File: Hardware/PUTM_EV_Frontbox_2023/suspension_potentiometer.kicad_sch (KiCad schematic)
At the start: 19 parts, among them U13 MCP6001, U9 MCP6N11-005

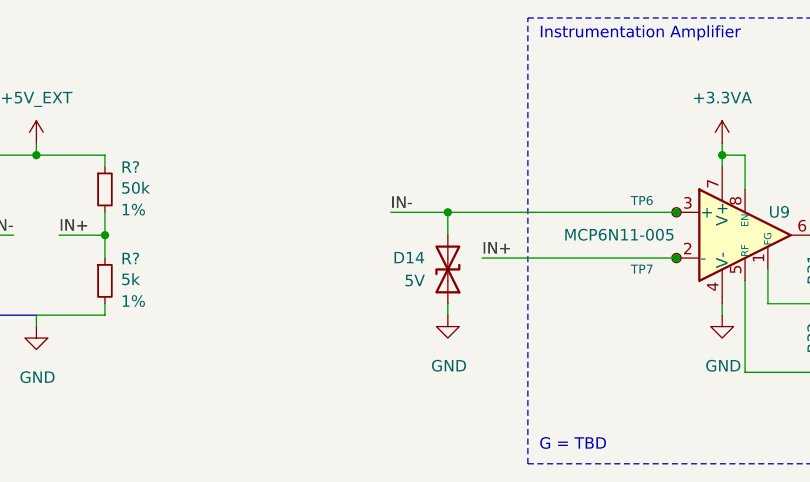
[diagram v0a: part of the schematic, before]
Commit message: Schematic updates
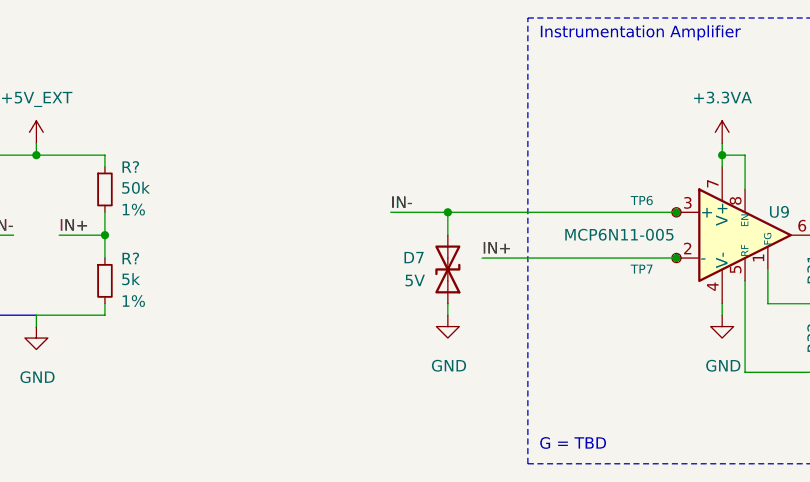
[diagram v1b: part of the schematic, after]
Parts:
- renumbered D14 to D7, NT4 to NT1
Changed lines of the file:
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@@
   (symbol (lib_id "Device:R_Small") (at 146.05 93.345 180) (unit 1)
     (in_bom yes) (on_board yes) (dnp no)
-    (property "Reference" "R?" (at 143.51 93.345 90)
+    (property "Reference" "R31" (at 143.51 93.345 90)
       (effects (font (size 1.27 1.27)))
     )
@@
   (symbol (lib_id "Connector:TestPoint_Small") (at 128.27 86.995 0) (unit 1)
     (in_bom yes) (on_board yes) (dnp no)
-    (property "Reference" "TP?" (at 123.19 85.725 0)
+    (property "Reference" "TP6" (at 123.19 85.725 0)
       (effects (font (size 1 1)) (justify left))
     )
@@
   (symbol (lib_id "power:GND") (at 182.88 100.965 0) (unit 1)
     (in_bom yes) (on_board yes) (dnp no)
-    (property "Reference" "#PWR?" (at 182.88 107.315 0)
+    (property "Reference" "#PWR033" (at 182.88 107.315 0)
       (effects (font (size 1.27 1.27)) hide)
     )
@@
   (symbol (lib_id "power:GND") (at 196.85 100.965 0) (unit 1)
     (in_bom yes) (on_board yes) (dnp no)
-    (property "Reference" "#PWR?" (at 196.85 107.315 0)
+    (property "Reference" "#PWR063" (at 196.85 107.315 0)
       (effects (font (size 1.27 1.27)) hide)
     )
@@
   (symbol (lib_id "power:GND") (at 102.87 98.425 0) (unit 1)
     (in_bom yes) (on_board yes) (dnp no)
-    (property "Reference" "#PWR?" (at 102.87 104.775 0)
+    (property "Reference" "#PWR024" (at 102.87 104.775 0)
       (effects (font (size 1.27 1.27)) hide)
     )
@@
   (symbol (lib_id "Device:R_Small") (at 163.83 89.535 90) (unit 1)
     (in_bom yes) (on_board yes) (dnp no)
-    (property "Reference" "R?" (at 163.83 86.995 90)
+    (property "Reference" "R33" (at 163.83 86.995 90)
       (effects (font (size 1.27 1.27)))
     )
@@
   (symbol (lib_id "power:GND") (at 133.35 98.425 0) (unit 1)
     (in_bom yes) (on_board yes) (dnp no)
-    (property "Reference" "#PWR?" (at 133.35 104.775 0)
+    (property "Reference" "#PWR030" (at 133.35 104.775 0)
       (effects (font (size 1.27 1.27)) hide)
     )
@@
   (symbol (lib_id "Device:NetTie_2") (at 46.99 89.535 0) (unit 1)
     (in_bom no) (on_board yes) (dnp no) (fields_autoplaced)
-    (property "Reference" "NT4" (at 46.99 84.455 0)
+    (property "Reference" "NT1" (at 46.99 84.455 0)
       (effects (font (size 1.27 1.27)) hide)
     )
@@
   (symbol (lib_id "MCP6N11:MCP6N11") (at 135.89 89.535 0) (unit 1)
     (in_bom yes) (on_board yes) (dnp no)
-    (property "Reference" "U?" (at 139.7 86.995 0)
+    (property "Reference" "U9" (at 139.7 86.995 0)
       (effects (font (size 1.27 1.27)))
     )
@@
   (symbol (lib_id "Amplifier_Operational:MCP6001-OT") (at 199.39 92.075 0) (unit 1)
     (in_bom yes) (on_board yes) (dnp no)
-    (property "Reference" "U?" (at 201.93 88.6461 0)
+    (property "Reference" "U13" (at 201.93 88.6461 0)
       (effects (font (size 1.27 1.27)))
     )
@@
   (symbol (lib_id "Connector:TestPoint_Small") (at 128.27 92.075 0) (mirror x) (unit 1)
     (in_bom yes) (on_board yes) (dnp no)
-    (property "Reference" "TP?" (at 123.19 93.345 0)
+    (property "Reference" "TP7" (at 123.19 93.345 0)
       (effects (font (size 1 1)) (justify left))
     )
@@
   (symbol (lib_id "Connector:TestPoint_Small") (at 208.28 92.075 0) (unit 1)
     (in_bom yes) (on_board yes) (dnp no)
-    (property "Reference" "TP?" (at 209.55 90.805 0)
+    (property "Reference" "TP9" (at 209.55 90.805 0)
       (effects (font (size 1 1)) (justify left))
     )
@@
   (symbol (lib_id "Device:R_Small") (at 146.05 100.965 180) (unit 1)
     (in_bom yes) (on_board yes) (dnp no)
-    (property "Reference" "R?" (at 143.51 100.965 90)
+    (property "Reference" "R32" (at 143.51 100.965 90)
       (effects (font (size 1.27 1.27)))
     )
@@
   (symbol (lib_id "power:GND") (at 241.3 97.155 0) (unit 1)
     (in_bom yes) (on_board yes) (dnp no)
-    (property "Reference" "#PWR?" (at 241.3 103.505 0)
+    (property "Reference" "#PWR092" (at 241.3 103.505 0)
       (effects (font (size 1.27 1.27)) hide)
     )
@@
   (symbol (lib_id "Device:R_Small") (at 173.99 89.535 90) (unit 1)
     (in_bom yes) (on_board yes) (dnp no)
-    (property "Reference" "R?" (at 173.99 86.995 90)
+    (property "Reference" "R34" (at 173.99 86.995 90)
       (effects (font (size 1.27 1.27)))
     )
@@
   (symbol (lib_id "Device:C_Small") (at 189.23 75.565 90) (unit 1)
     (in_bom yes) (on_board yes) (dnp no)
-    (property "Reference" "C?" (at 191.1413 71.755 90)
+    (property "Reference" "C21" (at 191.1413 71.755 90)
       (effects (font (size 1.27 1.27)) (justify left))
     )
@@
   (symbol (lib_id "Power_Ports:+5V_EXT") (at 57.15 79.375 0) (unit 1)
     (in_bom yes) (on_board yes) (dnp no)
-    (property "Reference" "#PWR051" (at 57.15 83.185 0)
+    (property "Reference" "#PWR019" (at 57.15 83.185 0)
       (effects (font (size 1.27 1.27)) hide)
     )
@@
   (symbol (lib_id "Device:C_Small") (at 182.88 95.885 0) (mirror y) (unit 1)
     (in_bom yes) (on_board yes) (dnp no)
-    (property "Reference" "C?" (at 180.34 95.2563 0)
+    (property "Reference" "C2" (at 180.34 95.2563 0)
       (effects (font (size 1.27 1.27)) (justify left))
     )
@@
   (symbol (lib_id "Device:D_TVS") (at 102.87 93.345 270) (mirror x) (unit 1)
     (in_bom yes) (on_board yes) (dnp no)
-    (property "Reference" "D14" (at 100.33 92.075 90)
+    (property "Reference" "D7" (at 100.33 92.075 90)
       (effects (font (size 1.27 1.27)) (justify right))
     )
@@
   (symbol (lib_id "Connector:TestPoint_Small") (at 146.05 89.535 0) (unit 1)
     (in_bom yes) (on_board yes) (dnp no)
-    (property "Reference" "TP?" (at 144.78 88.265 0)
+    (property "Reference" "TP8" (at 144.78 88.265 0)
       (effects (font (size 1 1)) (justify left))
     )
@@
   (symbol (lib_id "Device:C_Small") (at 246.38 92.075 0) (unit 1)
     (in_bom yes) (on_board yes) (dnp no)
-    (property "Reference" "C?" (at 248.92 91.4463 0)
+    (property "Reference" "C26" (at 248.92 91.4463 0)
       (effects (font (size 1.27 1.27)) (justify left))
     )
@@
   (symbol (lib_id "power:GND") (at 146.05 106.045 0) (unit 1)
     (in_bom yes) (on_board yes) (dnp no)
-    (property "Reference" "#PWR?" (at 146.05 112.395 0)
+    (property "Reference" "#PWR031" (at 146.05 112.395 0)
       (effects (font (size 1.27 1.27)) hide)
     )
@@
   (symbol (lib_id "Device:C_Small") (at 236.22 92.075 0) (unit 1)
     (in_bom yes) (on_board yes) (dnp no)
-    (property "Reference" "C?" (at 238.76 91.4463 0)
-      (effects (font (size 1.27 1.27)) (justify left))
-    )
+    (property "Reference" "C22" (at 238.76 91.4463 0)
+      (effects (font (size 1.27 1.27)) (justify left))
+    )

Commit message: Started PCB layout
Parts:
- removed NT1: NetTie_2, NetTie:NetTie-2_SMD_Pad0.5mm, symbol Device:NetTie_2
- C31: renamed from C26; footprint Capacitor_SMD:C_0603_1608Metric -> Capacitor_SMD:C_0402_1005Metric_Pad0.74x0.62mm_HandSolder
- renumbered C2 to C27, C21 to C28, C22 to C30, D7 to D8, R31 to R44, R32 to R45, R33 to R46, R34 to R47, TP6 to TP10, TP7 to TP11, TP8 to TP12, TP9 to TP13, U9 to U14, U13 to U15
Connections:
- net IN- is gone; now on net IN: D8.2 (A2), R?.2, TP10.1, U14.3 (+)

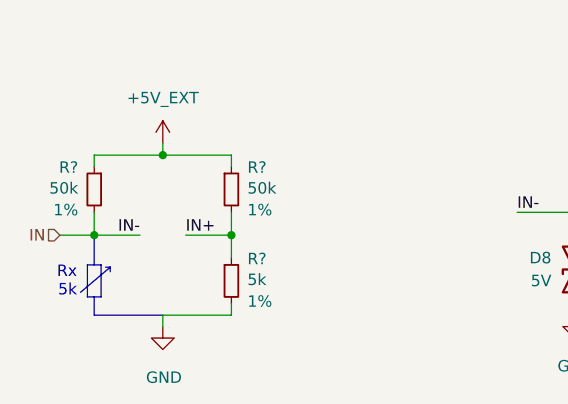
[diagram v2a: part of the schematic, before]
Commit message: Changed board outline and layout to match ASB
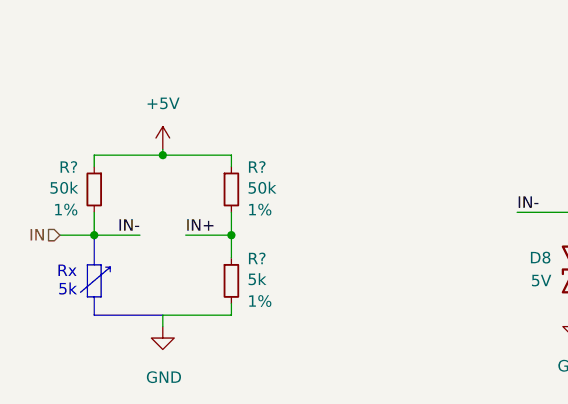
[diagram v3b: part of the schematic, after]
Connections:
- net +5V_EXT renamed +5V
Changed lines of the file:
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@@
     (stroke (width 0) (type default))
   )
-  (wire (pts (xy 57.15 79.375) (xy 57.15 80.645))
+  (wire (pts (xy 57.15 80.01) (xy 57.15 80.645))
     (stroke (width 0) (type default))
   )
@@
     )
   )
-  (symbol (lib_id "Power_Ports:+5V_EXT") (at 57.15 79.375 0) (unit 1)
-    (in_bom yes) (on_board yes) (dnp no)
-    (property "Reference" "#PWR093" (at 57.15 83.185 0)
-      (effects (font (size 1.27 1.27)) hide)
-    )
-    (property "Value" "+5V_EXT" (at 57.15 74.295 0)
-      (effects (font (size 1.27 1.27)))
-    )
-    (property "Footprint" "" (at 57.15 79.375 0)
-      (effects (font (size 1.27 1.27)) hide)
-    )
-    (property "Datasheet" "" (at 57.15 79.375 0)
-      (effects (font (size 1.27 1.27)) hide)
-    )
-    (pin "1")
-    (instances
-      (project "PUTM_EV_Frontbox_2023"
-        (path "/b652b05a-4e3d-4ad1-b032-18886abe7d45/911b86f7-6c1b-4cf5-8c52-4f515716b2b9"
-          (reference "#PWR093") (unit 1)
-        )
-        (path "/b652b05a-4e3d-4ad1-b032-18886abe7d45/cff9e037-b571-49da-8ef7-9a05892cc423"
-          (reference "#PWR019") (unit 1)
-        )
-        (path "/b652b05a-4e3d-4ad1-b032-18886abe7d45/9be5e515-3e18-403e-b27a-ea3087f1514f"
-          (reference "#PWR091") (unit 1)
-        )
-        (path "/b652b05a-4e3d-4ad1-b032-18886abe7d45/9e566fb6-1741-4092-b17e-402796433191"
-          (reference "#PWR0168") (unit 1)
-        )
-      )
-    )
-  )
   (symbol (lib_id "Device:C_Small") (at 182.88 95.885 0) (mirror y) (unit 1)
     (in_bom yes) (on_board yes) (dnp no)
@@
         )
       )
+    )
+  )
+  (symbol (lib_id "power:+5V") (at 57.15 80.01 0) (unit 1)
+    (in_bom yes) (on_board yes) (dnp no) (fields_autoplaced)
+    (property "Reference" "#PWR093" (at 57.15 83.82 0)
+      (effects (font (size 1.27 1.27)) hide)
+    )
+    (property "Value" "+5V" (at 57.15 74.93 0)
+      (effects (font (size 1.27 1.27)))
+    )
+    (property "Footprint" "" (at 57.15 80.01 0)
+      (effects (font (size 1.27 1.27)) hide)
+    )
+    (property "Datasheet" "" (at 57.15 80.01 0)
+      (effects (font (size 1.27 1.27)) hide)
+    )
+    (pin "1")
+    (instances
+      (project "PUTM_EV_Frontbox_2023"
+        (path "/b652b05a-4e3d-4ad1-b032-18886abe7d45/9e566fb6-1741-4092-b17e-402796433191"
+          (reference "#PWR093") (unit 1)
+        )
+        (path "/b652b05a-4e3d-4ad1-b032-18886abe7d45/cff9e037-b571-49da-8ef7-9a05892cc423"
+          (reference "#PWR04") (unit 1)
+        )
+        (path "/b652b05a-4e3d-4ad1-b032-18886abe7d45/911b86f7-6c1b-4cf5-8c52-4f515716b2b9"
+          (reference "#PWR019") (unit 1)
+        )
+        (path "/b652b05a-4e3d-4ad1-b032-18886abe7d45/9be5e515-3e18-403e-b27a-ea3087f1514f"
+          (reference "#PWR091") (unit 1)
+        )
+      )

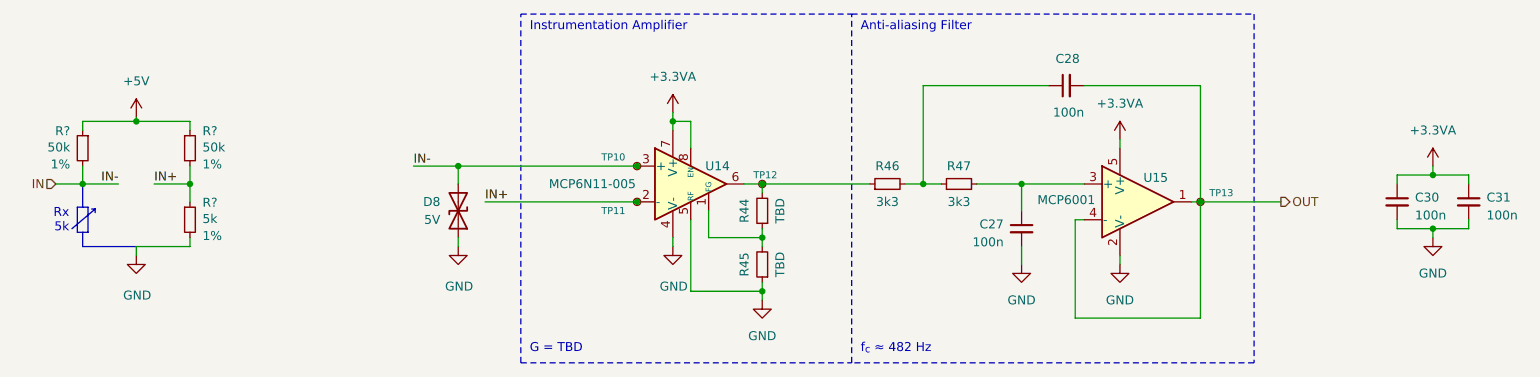
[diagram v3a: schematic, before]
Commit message: Added gearbox temperature sensors on schematic
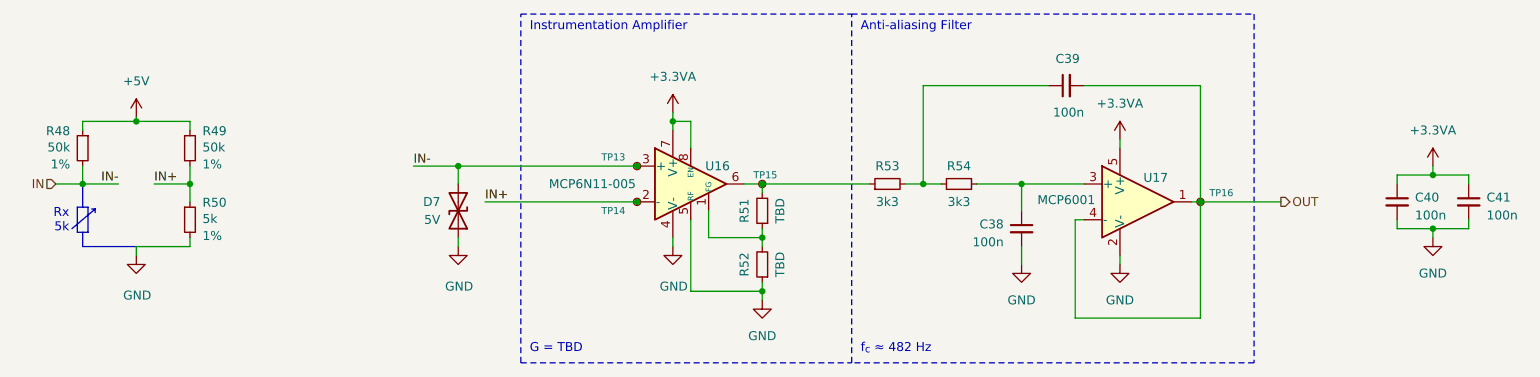
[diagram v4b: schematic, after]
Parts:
- gave numbers to parts that had none: 3
- renumbered C27 to C38, C28 to C39, C30 to C40, C31 to C41, D8 to D7, R44 to R51, R45 to R52, R46 to R53, R47 to R54, TP10 to TP13, TP11 to TP14, TP12 to TP15, TP13 to TP16, U14 to U16, U15 to U17
